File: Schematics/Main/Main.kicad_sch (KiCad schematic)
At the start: 3 parts, among them U1 PCM5102A, U2 PAM8403D

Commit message: Started Adding PCM5102 board schematic
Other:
- added sheet PCM5102A-Board (PCM5102A-Board.kicad_sch)
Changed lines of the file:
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@@
 (kicad_sch
-	(version 20231120)
+	(version 20250114)
 	(generator "eeschema")
-	(generator_version "8.0")
+	(generator_version "9.0")
 	(paper "A4")
 	(title_block
@@
 		)
 	)
+	(sheet
+		(at 201.93 115.57)
+		(size 38.1 25.4)
+		(exclude_from_sim no)
+		(in_bom yes)
+		(on_board yes)
+		(dnp no)
+		(fields_autoplaced yes)
+		(stroke
+			(width 0.1524)
+			(type solid)
+		)
+		(fill
+			(color 0 0 0 0.0000)
+		)
+		(property "Sheetname" "PCM5102A-Board"
+			(at 201.93 114.8584 0)
+			(effects
+				(font
+					(size 1.27 1.27)
+				)
+				(justify left bottom)
+			)
+		)
+		(property "Sheetfile" "PCM5102A-Board.kicad_sch"
+			(at 201.93 141.5546 0)
+			(effects
+				(font
+					(size 1.27 1.27)
+				)
+				(justify left top)
+			)
+		)
+		(pin "BCK" output
+			(at 201.93 121.92 180)
+			(effects
+				(font
+					(size 1.27 1.27)
+				)
+				(justify left)
+			)
+		)
+		(pin "DIN" output
+			(at 201.93 124.46 180)
+			(effects
+				(font
+					(size 1.27 1.27)
+				)
+				(justify left)
+			)
+		)
+		(pin "GND" output
+			(at 201.93 127 180)
+			(effects
+				(font
+					(size 1.27 1.27)
+				)
+				(justify left)
+			)
+		)
+		(pin "LRCK" output
+			(at 201.93 129.54 180)
+			(effects
+				(font
+					(size 1.27 1.27)
+				)
+				(justify left)
+			)
+		)
+		(pin "SCK" output
+			(at 201.93 132.08 180)
+			(effects
+				(font
+					(size 1.27 1.27)
+				)
+				(justify left)
+			)
+		)
+		(pin "VIN" output
+			(at 201.93 134.62 180)
+			(effects
+				(font
+					(size 1.27 1.27)
+				)
+				(justify left)
+			)
+		)
+		(instances
+			(project "Main"
+				(path "/2b6c83b8-b6db-46e9-a845-f7ffa0649aa2"
+					(page "2")
+				)
+			)
+		)
+	)
 	(sheet_instances
 		(path "/"
@@
 		)
 	)
+	(embedded_fonts no)
 )

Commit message: Continue on Laptop
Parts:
- removed R1: R, symbol Device:R
- removed U1: PCM5102A, Package_SO:TSSOP-20_4.4x6.5mm_P0.65mm, symbol Audio:PCM5102A
- removed U2: PAM8403D, Package_SO:SOP-16_3.9x9.9mm_P1.27mm, symbol Amplifier_Audio:PAM8403D
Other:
- added sheet PAM8403-Board (PAM8403-Board.kicad_sch)
- sheet PCM5102A-Board ports: added A3V3, AGND, DEMP, FLT, FMT, LOUT, ROUT, XSMT; removed none
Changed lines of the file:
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@@
 		(date "2025-02-21")
 	)
-	(symbol
-		(lib_id "Amplifier_Audio:PAM8403D")
-		(at 154.94 78.74 0)
-		(unit 1)
+	(sheet
+		(at 64.77 68.58)
+		(size 27.94 19.05)
 		(exclude_from_sim no)
 		(in_bom yes)
@@
 		(dnp no)
 		(fields_autoplaced yes)
-		(property "Reference" "U2"
-			(at 157.1341 60.96 0)
-			(effects
-				(font
-					(size 1.27 1.27)
-				)
-				(justify left)
-			)
-		)
-		(property "Value" "PAM8403D"
-			(at 157.1341 63.5 0)
-			(effects
-				(font
-					(size 1.27 1.27)
-				)
-				(justify left)
-			)
-		)
-		(property "Footprint" "Package_SO:SOP-16_3.9x9.9mm_P1.27mm"
-			(at 154.94 78.74 0)
-			(effects
-				(font
-					(size 1.27 1.27)
-				)
-				(hide yes)
-			)
-		)
-		(property "Datasheet" "https://www.diodes.com/assets/Datasheets/products_inactive_data/PAM8403.pdf"
-			(at 149.86 73.66 0)
-			(effects
-				(font
-					(size 1.27 1.27)
-				)
-				(hide yes)
-			)
-		)
-		(property "Description" "3W Filterless Class-D Stereo Audio Amplifier, SOP-16"
-			(at 154.94 78.74 0)
-			(effects
-				(font
-					(size 1.27 1.27)
-				)
-				(hide yes)
-			)
-		)
-		(pin "13"
-		)
-		(pin "11"
-		)
-		(pin "5"
-		)
-		(pin "2"
-		)
-		(pin "4"
-		)
-		(pin "16"
-		)
-		(pin "14"
-		)
-		(pin "7"
-		)
-		(pin "15"
-		)
-		(pin "6"
-		)
-		(pin "8"
-		)
-		(pin "12"
-		)
-		(pin "10"
-		)
-		(pin "3"
-		)
-		(pin "9"
-		)
-		(pin "1"
+		(stroke
+			(width 0.1524)
+			(type solid)
+		)
+		(fill
+			(color 0 0 0 0.0000)
+		)
+		(property "Sheetname" "PAM8403-Board"
+			(at 64.77 67.8684 0)
+			(effects
+				(font
+					(size 1.27 1.27)
+				)
+				(justify left bottom)
+			)
+		)
+		(property "Sheetfile" "PAM8403-Board.kicad_sch"
+			(at 64.77 88.2146 0)
+			(effects
+				(font
+					(size 1.27 1.27)
+				)
+				(justify left top)
+			)
 		)
 		(instances
-			(project ""
+			(project "Main"
 				(path "/2b6c83b8-b6db-46e9-a845-f7ffa0649aa2"
-					(reference "U2")
-					(unit 1)
-				)
-			)
-		)
-	)
-	(symbol
-		(lib_id "Audio:PCM5102A")
-		(at 82.55 104.14 0)
-		(unit 1)
-		(exclude_from_sim no)
-		(in_bom yes)
-		(on_board yes)
-		(dnp no)
-		(property "Reference" "U1"
-			(at 150.7841 88.9 0)
-			(effects
-				(font
-					(size 1.27 1.27)
-				)
-				(justify left)
-			)
-		)
-		(property "Value" "PCM5102A"
-			(at 150.7841 91.44 0)
-			(effects
-				(font
-					(size 1.27 1.27)
-				)
-				(justify left)
-			)
-		)
-		(property "Footprint" "Package_SO:TSSOP-20_4.4x6.5mm_P0.65mm"
-			(at 107.95 120.65 0)
-			(effects
-				(font
-					(size 1.27 1.27)
-				)
-				(hide yes)
-			)
-		)
-		(property "Datasheet" "https://www.ti.com/lit/ds/symlink/pcm5102a.pdf"
-			(at 82.55 104.14 0)
-			(effects
-				(font
-					(size 1.27 1.27)
-				)
-				(hide yes)
-			)
-		)
-		(property "Description" "2.1 VRMS, 112dB Audio Stereo DAC with PLL and 32-bit, 384kHz PCM Interface, TSSOP-20"
-			(at 82.55 104.14 0)
-			(effects
-				(font
-					(size 1.27 1.27)
-				)
-				(hide yes)
-			)
-		)
-		(pin "2"
-		)
-		(pin "18"
-		)
-		(pin "12"
-		)
-		(pin "20"
-		)
-		(pin "8"
-		)
-		(pin "5"
-		)
-		(pin "7"
-		)
-		(pin "4"
-		)
-		(pin "1"
-		)
-		(pin "13"
-		)
-		(pin "9"
-		)
-		(pin "3"
-		)
-		(pin "15"
-		)
-		(pin "6"
-		)
-		(pin "10"
-		)
-		(pin "14"
-		)
-		(pin "19"
-		)
-		(pin "11"
-		)
-		(pin "16"
-		)
-		(pin "17"
-		)
-		(instances
-			(project ""
-				(path "/2b6c83b8-b6db-46e9-a845-f7ffa0649aa2"
-					(reference "U1")
-					(unit 1)
-				)
-			)
-		)
-	)
-	(symbol
-		(lib_id "Device:R")
-		(at 124.46 90.17 0)
-		(unit 1)
-		(exclude_from_sim no)
-		(in_bom yes)
-		(on_board yes)
-		(dnp no)
-		(fields_autoplaced yes)
-		(property "Reference" "R1"
-			(at 127 88.8999 0)
-			(effects
-				(font
-					(size 1.27 1.27)
-				)
-				(justify left)
-			)
-		)
-		(property "Value" "R"
-			(at 127 91.4399 0)
-			(effects
-				(font
-					(size 1.27 1.27)
-				)
-				(justify left)
-			)
-		)
-		(property "Footprint" ""
-			(at 122.682 90.17 90)
-			(effects
-				(font
-					(size 1.27 1.27)
-				)
-				(hide yes)
-			)
-		)
-		(property "Datasheet" "~"
-			(at 124.46 90.17 0)
-			(effects
-				(font
-					(size 1.27 1.27)
-				)
-				(hide yes)
-			)
-		)
-		(property "Description" "Resistor"
-			(at 124.46 90.17 0)
-			(effects
-				(font
-					(size 1.27 1.27)
-				)
-				(hide yes)
-			)
-		)
-		(pin "2"
-		)
-		(pin "1"
-		)
-		(instances
-			(project ""
-				(path "/2b6c83b8-b6db-46e9-a845-f7ffa0649aa2"
-					(reference "R1")
-					(unit 1)
+					(page "3")
 				)
 			)
@@
 			)
 		)
+		(pin "A3V3" output
+			(at 240.03 120.65 0)
+			(effects
+				(font
+					(size 1.27 1.27)
+				)
+				(justify right)
+			)
+		)
+		(pin "AGND" output
+			(at 240.03 125.73 0)
+			(effects
+				(font
+					(size 1.27 1.27)
+				)
+				(justify right)
+			)
+		)
+		(pin "DEMP" input
+			(at 219.71 115.57 90)
+			(effects
+				(font
+					(size 1.27 1.27)
+				)
+				(justify right)
+			)
+		)
+		(pin "FLT" input
+			(at 222.25 115.57 90)
+			(effects
+				(font
+					(size 1.27 1.27)
+				)
+				(justify right)
+			)
+		)
+		(pin "FMT" input
+			(at 224.79 115.57 90)
+			(effects
+				(font
+					(size 1.27 1.27)
+				)
+				(justify right)
+			)
+		)
+		(pin "LOUT" output
+			(at 240.03 123.19 0)
+			(effects
+				(font
+					(size 1.27 1.27)
+				)
+				(justify right)
+			)
+		)
+		(pin "ROUT" output
+			(at 240.03 128.27 0)
+			(effects
+				(font
+					(size 1.27 1.27)
+				)
+				(justify right)
+			)
+		)
+		(pin "XSMT" input
+			(at 227.33 115.57 90)
+			(effects
+				(font
+					(size 1.27 1.27)
+				)
+				(justify right)
+			)
+		)

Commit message: Addendum
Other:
- sheet PAM8403-Board ports: added 5V, GND, GNDIN, LIN, LOUT+, LOUT-, RIN, ROUT+, ROUT-; removed none
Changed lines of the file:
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@@
+			)
+		)
+		(pin "5V" input
+			(at 64.77 71.12 180)
+			(effects
+				(font
+					(size 1.27 1.27)
+				)
+				(justify left)
+			)
+		)
+		(pin "GND" input
+			(at 64.77 73.66 180)
+			(effects
+				(font
+					(size 1.27 1.27)
+				)
+				(justify left)
+			)
+		)
+		(pin "GNDIN" input
+			(at 64.77 82.55 180)
+			(effects
+				(font
+					(size 1.27 1.27)
+				)
+				(justify left)
+			)
+		)
+		(pin "LIN" input
+			(at 64.77 85.09 180)
+			(effects
+				(font
+					(size 1.27 1.27)
+				)
+				(justify left)
+			)
+		)
+		(pin "LOUT+" output
+			(at 92.71 85.09 0)
+			(effects
+				(font
+					(size 1.27 1.27)
+				)
+				(justify right)
+			)
+		)
+		(pin "LOUT-" output
+			(at 92.71 82.55 0)
+			(effects
+				(font
+					(size 1.27 1.27)
+				)
+				(justify right)
+			)
+		)
+		(pin "RIN" input
+			(at 64.77 80.01 180)
+			(effects
+				(font
+					(size 1.27 1.27)
+				)
+				(justify left)
+			)
+		)
+		(pin "ROUT+" output
+			(at 92.71 71.12 0)
+			(effects
+				(font
+					(size 1.27 1.27)
+				)
+				(justify right)
+			)
+		)
+		(pin "ROUT-" output
+			(at 92.71 73.66 0)
+			(effects
+				(font
+					(size 1.27 1.27)
+				)
+				(justify right)
 			)
 		)

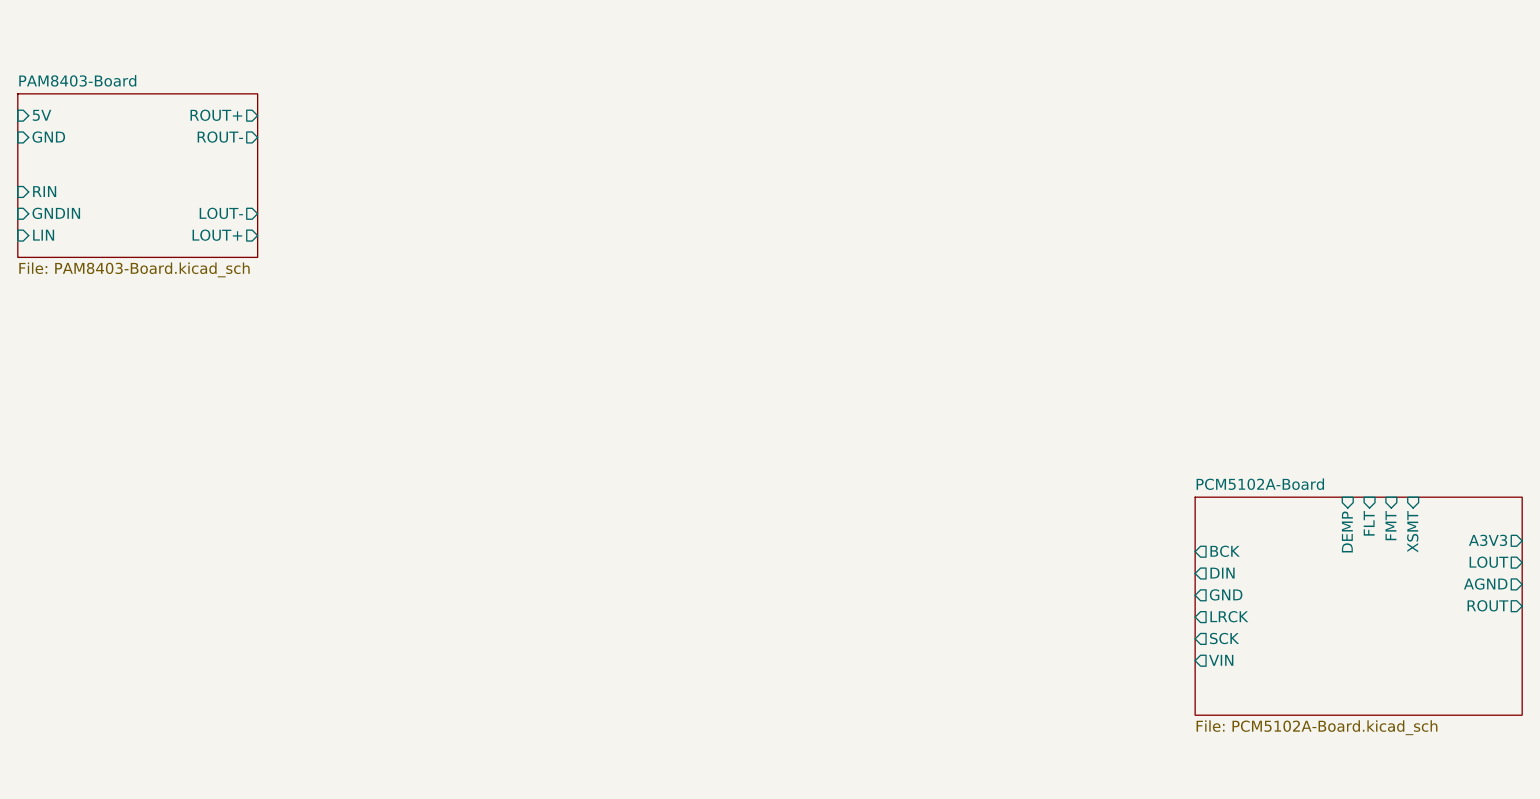
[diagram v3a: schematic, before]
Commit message: Added Audiosystem schematic
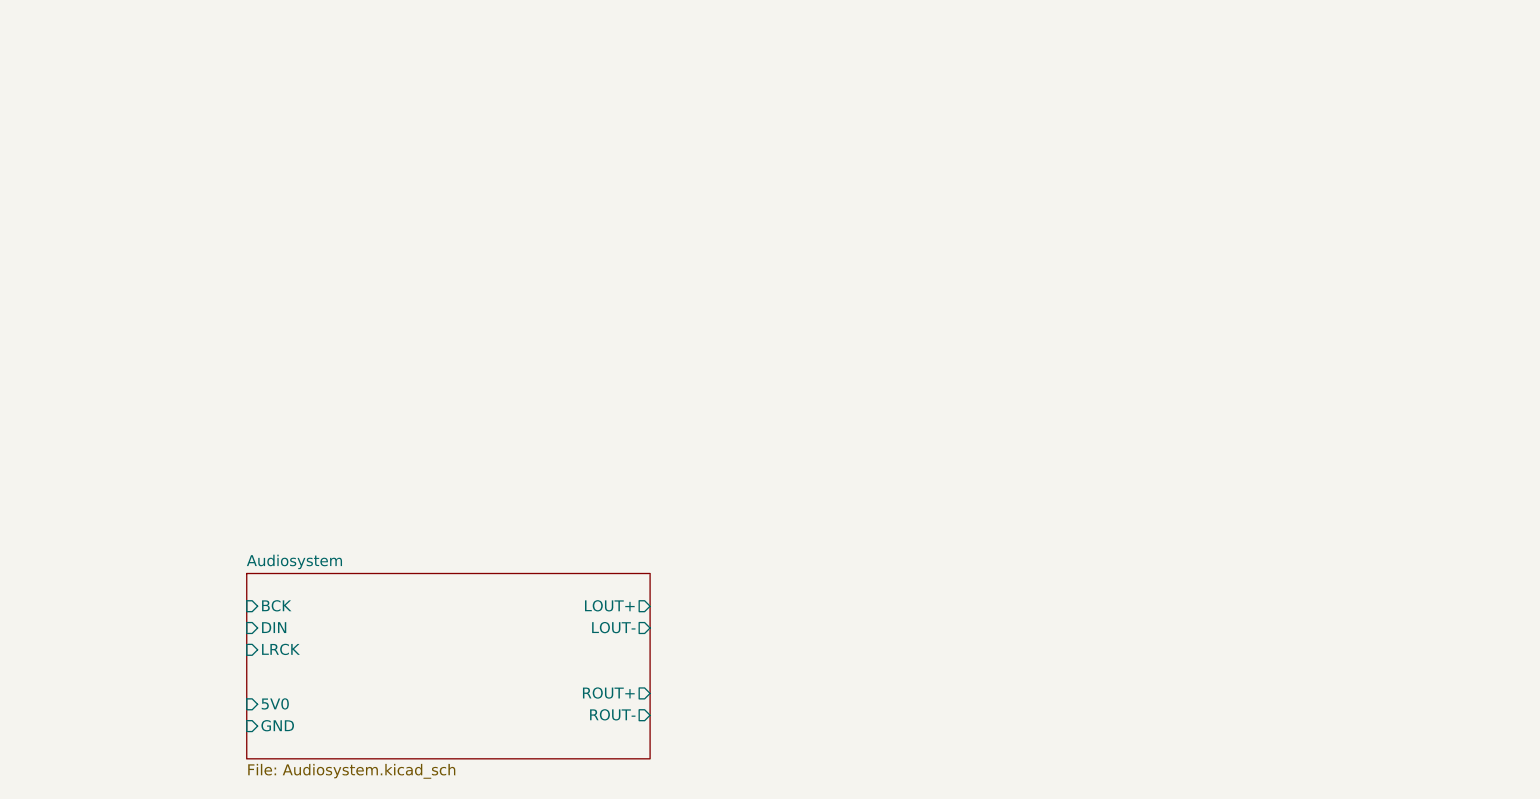
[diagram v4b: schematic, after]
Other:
- removed sheet PAM8403-Board
- removed sheet PCM5102A-Board
- added sheet Audiosystem (Audiosystem.kicad_sch)
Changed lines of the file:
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@@
 	)
 	(sheet
-		(at 64.77 68.58)
-		(size 27.94 19.05)
+		(at 91.44 124.46)
+		(size 46.99 21.59)
 		(exclude_from_sim no)
 		(in_bom yes)
@@
 			(color 0 0 0 0.0000)
 		)
-		(property "Sheetname" "PAM8403-Board"
-			(at 64.77 67.8684 0)
+		(property "Sheetname" "Audiosystem"
+			(at 91.44 123.7484 0)
 			(effects
 				(font
@@
 			)
 		)
-		(property "Sheetfile" "PAM8403-Board.kicad_sch"
-			(at 64.77 88.2146 0)
+		(property "Sheetfile" "Audiosystem.kicad_sch"
+			(at 91.44 146.6346 0)
 			(effects
 				(font
@@
 			)
 		)
-		(pin "5V" input
-			(at 64.77 71.12 180)
+		(pin "BCK" input
+			(at 91.44 128.27 180)
+			(effects
+				(font
+					(size 1.27 1.27)
+				)
+				(justify left)
+			)
+		)
+		(pin "DIN" input
+			(at 91.44 130.81 180)
+			(effects
+				(font
+					(size 1.27 1.27)
+				)
+				(justify left)
+			)
+		)
+		(pin "LOUT+" output
+			(at 138.43 128.27 0)
+			(effects
+				(font
+					(size 1.27 1.27)
+				)
+				(justify right)
+			)
+		)
+		(pin "LOUT-" output
+			(at 138.43 130.81 0)
+			(effects
+				(font
+					(size 1.27 1.27)
+				)
+				(justify right)
+			)
+		)
+		(pin "LRCK" input
+			(at 91.44 133.35 180)
+			(effects
+				(font
+					(size 1.27 1.27)
+				)
+				(justify left)
+			)
+		)
+		(pin "ROUT+" output
+			(at 138.43 138.43 0)
+			(effects
+				(font
+					(size 1.27 1.27)
+				)
+				(justify right)
+			)
+		)
+		(pin "ROUT-" output
+			(at 138.43 140.97 0)
+			(effects
+				(font
+					(size 1.27 1.27)
+				)
+				(justify right)
+			)
+		)
+		(pin "5V0" input
+			(at 91.44 139.7 180)
 			(effects
 				(font
@@
 		)
 		(pin "GND" input
-			(at 64.77 73.66 180)
+			(at 91.44 142.24 180)
 			(effects
 				(font
@@
 			)
 		)
-		(pin "GNDIN" input
-			(at 64.77 82.55 180)
-			(effects
-				(font
-					(size 1.27 1.27)
-				)
-				(justify left)
-			)
-		)
-		(pin "LIN" input
-			(at 64.77 85.09 180)
-			(effects
-				(font
-					(size 1.27 1.27)
-				)
-				(justify left)
-			)
-		)
-		(pin "LOUT+" output
-			(at 92.71 85.09 0)
-			(effects
-				(font
-					(size 1.27 1.27)
-				)
-				(justify right)
-			)
-		)
-		(pin "LOUT-" output
-			(at 92.71 82.55 0)
-			(effects
-				(font
-					(size 1.27 1.27)
-				)
-				(justify right)
-			)
-		)
-		(pin "RIN" input
-			(at 64.77 80.01 180)
-			(effects
-				(font
-					(size 1.27 1.27)
-				)
-				(justify left)
-			)
-		)
-		(pin "ROUT+" output
-			(at 92.71 71.12 0)
-			(effects
-				(font
-					(size 1.27 1.27)
-				)
-				(justify right)
-			)
-		)
-		(pin "ROUT-" output
-			(at 92.71 73.66 0)
-			(effects
-				(font
-					(size 1.27 1.27)
-				)
-				(justify right)
-			)
-		)
-		(instances
-			(project "Main"
-				(path "/2b6c83b8-b6db-46e9-a845-f7ffa0649aa2"
-					(page "3")
-				)
-			)
-		)
-	)
-	(sheet
-		(at 201.93 115.57)
-		(size 38.1 25.4)
-		(exclude_from_sim no)
-		(in_bom yes)
-		(on_board yes)
-		(dnp no)
-		(fields_autoplaced yes)
-		(stroke
-			(width 0.1524)
-			(type solid)
-		)
-		(fill
-			(color 0 0 0 0.0000)
-		)
-		(property "Sheetname" "PCM5102A-Board"
-			(at 201.93 114.8584 0)
-			(effects
-				(font
-					(size 1.27 1.27)
-				)
-				(justify left bottom)
-			)
-		)
-		(property "Sheetfile" "PCM5102A-Board.kicad_sch"
-			(at 201.93 141.5546 0)
-			(effects
-				(font
-					(size 1.27 1.27)
-				)
-				(justify left top)
-			)
-		)
-		(pin "BCK" output
-			(at 201.93 121.92 180)
-			(effects
-				(font
-					(size 1.27 1.27)
-				)
-				(justify left)
-			)
-		)
-		(pin "DIN" output
-			(at 201.93 124.46 180)
-			(effects
-				(font
-					(size 1.27 1.27)
-				)
-				(justify left)
-			)
-		)
-		(pin "GND" output
-			(at 201.93 127 180)
-			(effects
-				(font
-					(size 1.27 1.27)
-				)
-				(justify left)
-			)
-		)
-		(pin "LRCK" output
-			(at 201.93 129.54 180)
-			(effects
-				(font
-					(size 1.27 1.27)
-				)
-				(justify left)
-			)
-		)
-		(pin "SCK" output
-			(at 201.93 132.08 180)
-			(effects
-				(font
-					(size 1.27 1.27)
-				)
-				(justify left)
-			)
-		)
-		(pin "VIN" output
-			(at 201.93 134.62 180)
-			(effects
-				(font
-					(size 1.27 1.27)
-				)
-				(justify left)
-			)
-		)
-		(pin "A3V3" output
-			(at 240.03 120.65 0)
-			(effects
-				(font
-					(size 1.27 1.27)
-				)
-				(justify right)
-			)
-		)
-		(pin "AGND" output
-			(at 240.03 125.73 0)
-			(effects
-				(font
-					(size 1.27 1.27)
-				)
-				(justify right)
-			)
-		)
-		(pin "DEMP" input
-			(at 219.71 115.57 90)
-			(effects
-				(font
-					(size 1.27 1.27)
-				)
-				(justify right)
-			)
-		)
-		(pin "FLT" input
-			(at 222.25 115.57 90)
-			(effects
-				(font
-					(size 1.27 1.27)
-				)
-				(justify right)
-			)
-		)
-		(pin "FMT" input
-			(at 224.79 115.57 90)
-			(effects
-				(font
-					(size 1.27 1.27)
-				)
-				(justify right)
-			)
-		)
-		(pin "LOUT" output
-			(at 240.03 123.19 0)
-			(effects
-				(font
-					(size 1.27 1.27)
-				)
-				(justify right)
-			)
-		)
-		(pin "ROUT" output
-			(at 240.03 128.27 0)
-			(effects
-				(font
-					(size 1.27 1.27)
-				)
-				(justify right)
-			)
-		)
-		(pin "XSMT" input
-			(at 227.33 115.57 90)
-			(effects
-				(font
-					(size 1.27 1.27)
-				)
-				(justify right)
-			)
-		)
